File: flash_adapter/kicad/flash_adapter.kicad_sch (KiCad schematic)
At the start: 7 parts, among them J1 Conn_01x10, J2 Conn_01x10, J3 DS1044-160G, SW1 MK-12C02-G020

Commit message: Updated flash adapter
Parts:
- removed SW1: MK-12C02-G020, C5-Addon:SW-SMD_MK-12C02-G020, symbol C5-Addon:MK-12C02-G020
- added R2, R3: 10k, Resistor_SMD:R_0805_2012Metric, symbol Device:R
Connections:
- net IO10 is gone; now on net MISO: J1.9 (Pin_9), J2.9 (Pin_9)
- net IO6 is gone; now on net MOSI: J1.6 (Pin_6), J2.6 (Pin_6)
- net IO8 is gone; now on net CS: J1.7 (Pin_7), J2.7 (Pin_7)
- net IO9 is gone; now on net SCLK: J1.8 (Pin_8), J2.8 (Pin_8)
- net UART_RX is gone; now on net WP: J1.5 (Pin_5), J2.5 (Pin_5)
- net UART_TX is gone; now on net HOLD: J1.4 (Pin_4), J2.4 (Pin_4)
- net VOUT is gone; now on net VIO_{DOCK}: R1.1
- net GND: now also C1.2, J3.4, J3.8
- net VIO_{DOCK}: now also C1.1, J3.12, J3.16, R2.2, R3.2
- net CS: now reaches J3.1
- net CS: now also J3.5
- net SCLK: now reaches J3.10
- net SCLK: now also J3.14
- net HOLD: now reaches J3.11
- net HOLD: now also J3.15, R3.1
- net MISO: now reaches J3.13
- net MISO: now also J3.9
- net MOSI: now reaches J3.2
- net MOSI: now also J3.6
- net WP: now reaches J3.3
- net WP: now also J3.7, R2.1
- net BOOT: no longer names the net of J1.3 (Pin_3), J2.3 (Pin_3)
- net RST: no longer names the net of J1.2 (Pin_2), J2.2 (Pin_2)
- no-connect marks 1 -> 0
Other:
- note added: "Bottom Half"
- note added: "Top Half"
- moved on the sheet: C1, D1, J1, J2, J3, R1

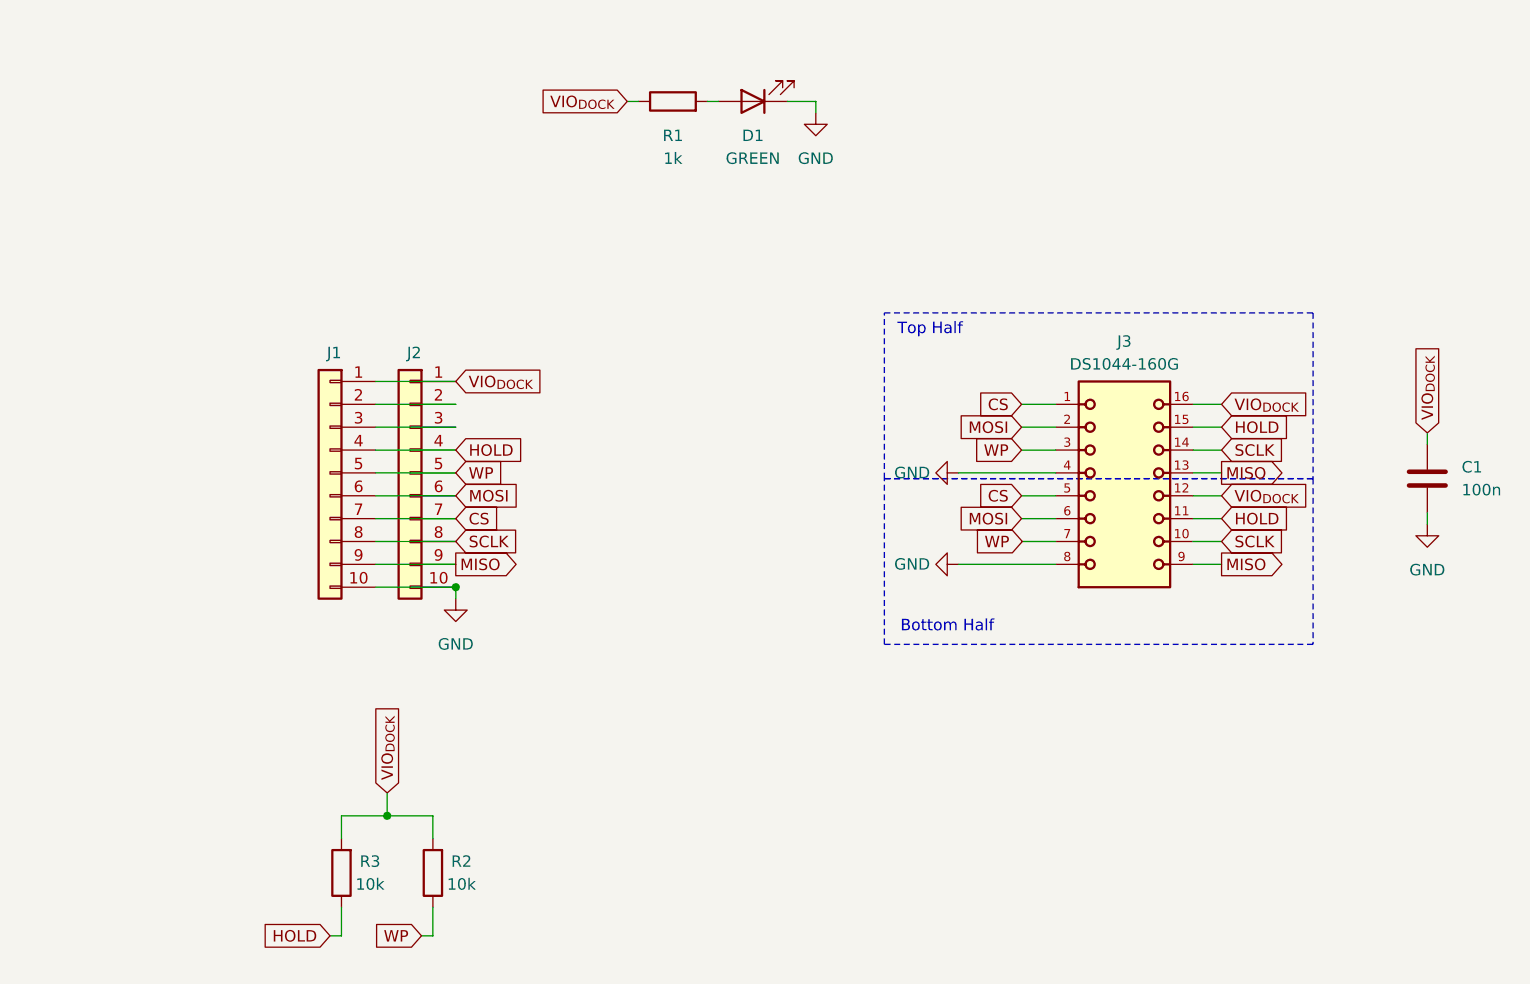
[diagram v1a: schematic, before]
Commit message: Added separate CS#
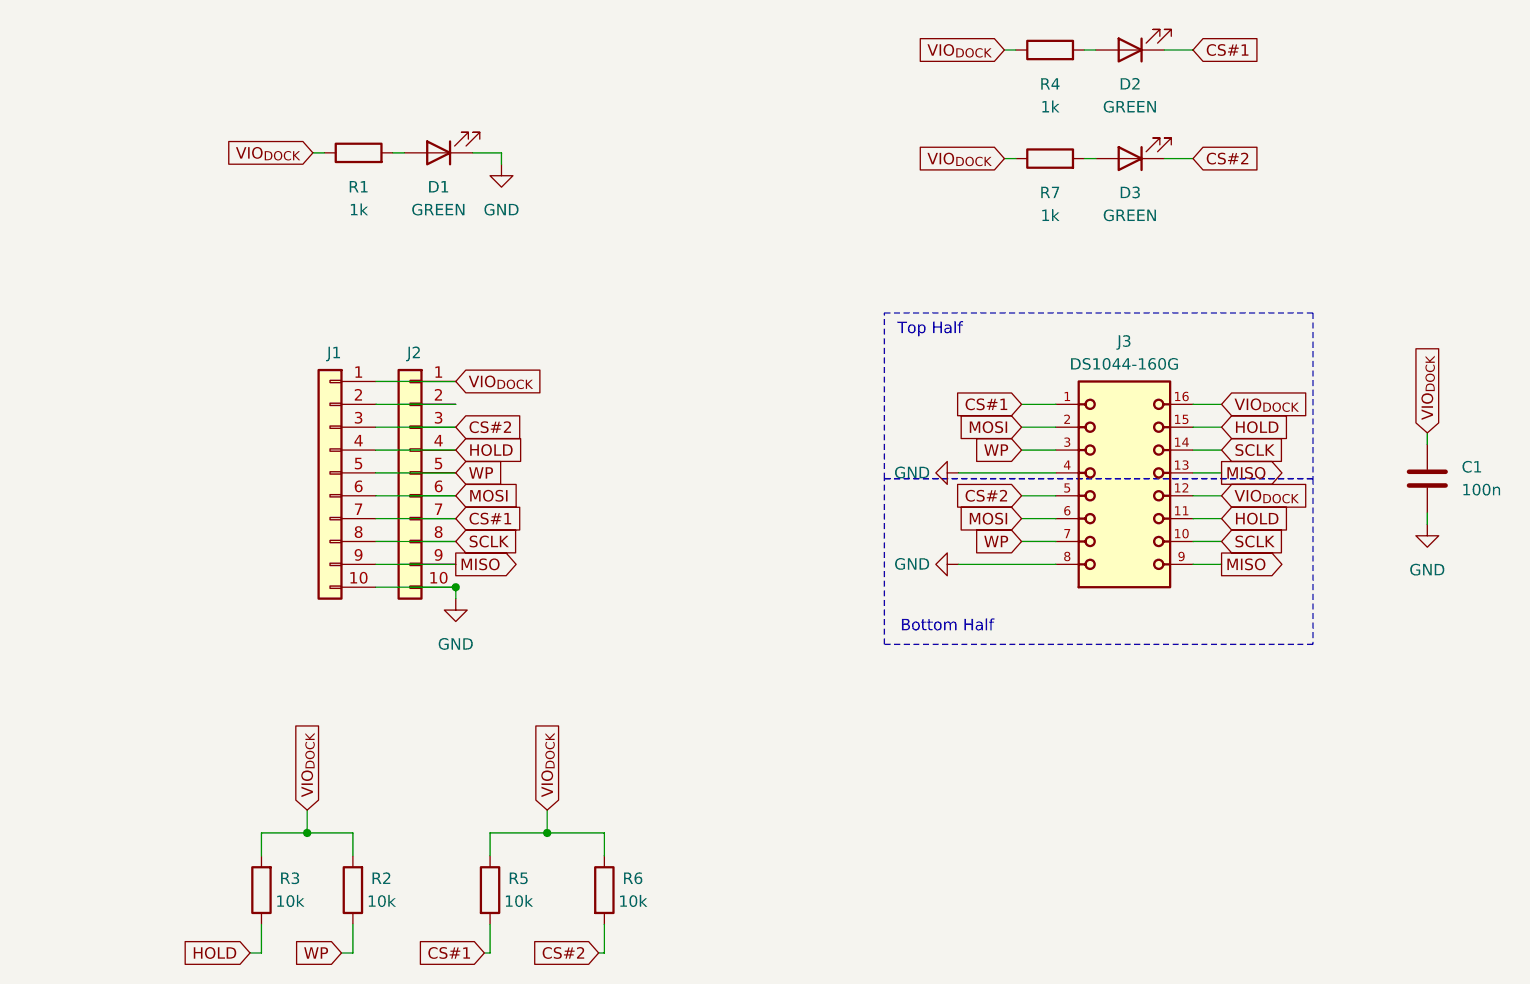
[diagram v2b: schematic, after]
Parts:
- added D2, D3: GREEN, LED_SMD:LED_0805_2012Metric, symbol Device:LED
- added R4, R7: 1k, Resistor_SMD:R_0805_2012Metric, symbol Device:R
- added R5, R6: 10k, Resistor_SMD:R_0805_2012Metric, symbol Device:R
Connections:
- net VIO_{DOCK}: now also R4.1, R5.1, R6.1, R7.1
- net CS#2: now reaches J1.3 (Pin_3), J2.3 (Pin_3)
- net CS#2: now also J3.5, D3.1 (K), R6.2
- net CS renamed CS#1
- net CS#1: now also D2.1 (K), R5.2; no longer J3.5
- new net: D3.2 (A), R7.2
- new net: D2.2 (A), R4.2
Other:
- moved on the sheet: D1, R1, R2, R3

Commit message: Finished routing
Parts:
- added D4: BLUE, LED_SMD:LED_0805_2012Metric, symbol Device:LED
- added R8: 1k, Resistor_SMD:R_0805_2012Metric, symbol Device:R
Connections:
- net CS#1: now also J1.3 (Pin_3), J2.3 (Pin_3); no longer J1.7 (Pin_7), J2.7 (Pin_7)
- net CS#2: now also J1.7 (Pin_7), J2.7 (Pin_7); no longer J1.3 (Pin_3), J2.3 (Pin_3)
- net GND: now also D4.1 (K)
- net IO13: now reaches J1.2 (Pin_2), J2.2 (Pin_2)
- net IO13: now also R8.1
- new net: D4.2 (A), R8.2
